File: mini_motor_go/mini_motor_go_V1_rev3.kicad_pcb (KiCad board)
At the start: 4 copper layers, 72 x 47 mm, 83 parts, among them J1 CONN_03POLAR_LOCK, J10 Conn_01x02_Pin, J11 USB4520-03-0-A_REVA, J12 BM05B-SRSS-TB_LF__SN_, J13 BM05B-SRSS-TB_LF__SN_, J2 CONN_03POLAR_LOCK, J3 I2C_STANDARDQWIIC, J5 I2C_STANDARDQWIIC, J9 Conn_01x09_Pin, U1 ESP32-S3-WROOM-1, U2 TMC6300, U3 INA2181, U4 INA2181, U5 TMC6300, U6 AZ1117C, U7 TPS562208

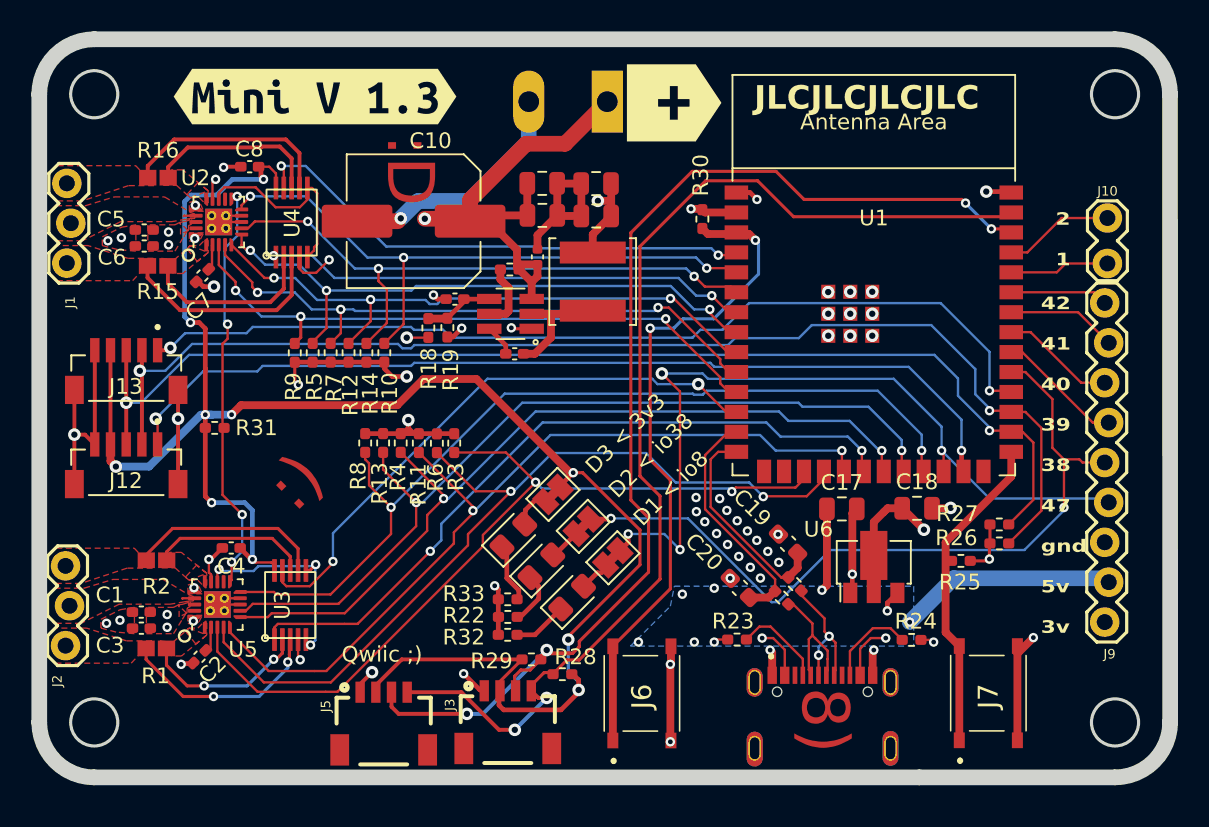
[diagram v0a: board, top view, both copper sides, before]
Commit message: reviewed value table in schematics, updated footprints on board minor improvements
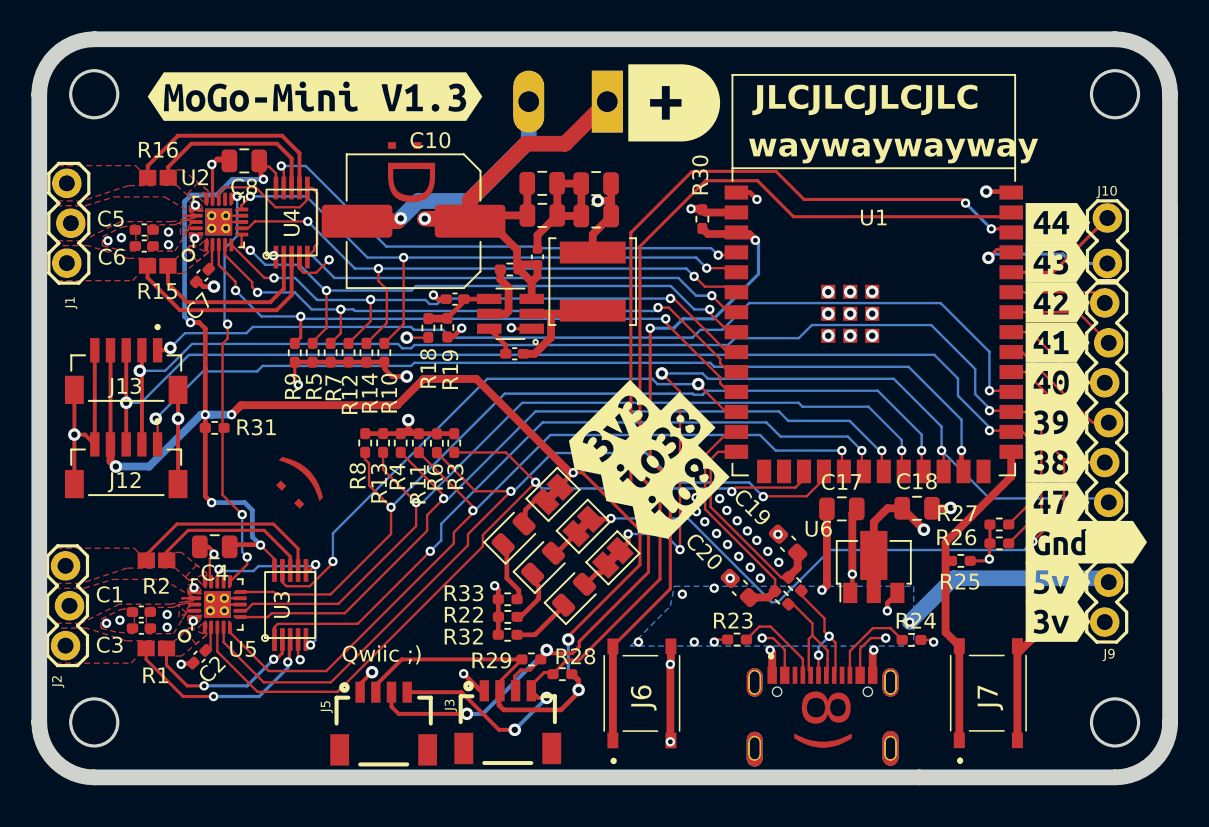
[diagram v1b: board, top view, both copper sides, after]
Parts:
- removed D1 < io8: LED, mg_mini_v1r3:LED_0805_2012Metric_Pad1.15x1.40mm_HandSolder
- removed D2 < io38: LED, mg_mini_v1r3:LED_0805_2012Metric_Pad1.15x1.40mm_HandSolder
- removed D3 < 3v3: LED, mg_mini_v1r3:LED_0805_2012Metric_Pad1.15x1.40mm_HandSolder
- removed kibuzzard-656F4911: G***, mg_mini_v1r3:kibuzzard-656F4911
- removed kibuzzard-656F59A7: G***, mg_mini_v1r3:kibuzzard-656F59A7
- added D1: LED, LED_SMD:LED_0805_2012Metric, F.Cu at (148.6, 84.9)
- added D2: LED, LED_SMD:LED_0805_2012Metric, F.Cu at (146.6, 82.9)
- added D3: LED, LED_SMD:LED_0805_2012Metric, F.Cu at (144.7, 81.0)
- added kibuzzard-6573395A: G***, kibuzzard-6573395A, F.Cu at (150.9, 74.6)
- added kibuzzard-65733965: G***, kibuzzard-65733965, F.Cu at (153.5, 76.0)
- added kibuzzard-65733972: G***, kibuzzard-65733972, F.Cu at (155.0, 78.6)
- added kibuzzard-65733A0D: G***, kibuzzard-65733A0D, F.Cu at (179.3, 63.7)
- added kibuzzard-65733A1B: G***, kibuzzard-65733A1B, F.Cu at (179.4, 61.2)
- added kibuzzard-65733C02: G***, kibuzzard-65733C02, F.Cu at (179.4, 66.3)
- added kibuzzard-65733C12: G***, kibuzzard-65733C12, F.Cu at (179.3, 68.8)
- added kibuzzard-65733C20: G***, kibuzzard-65733C20, F.Cu at (179.4, 71.4)
- added kibuzzard-65733C2B: G***, kibuzzard-65733C2B, F.Cu at (179.3, 73.9)
- added kibuzzard-65733C3A: G***, kibuzzard-65733C3A, F.Cu at (179.3, 76.4)
- added kibuzzard-65733C45: G***, kibuzzard-65733C45, F.Cu at (179.3, 79.0)
- added kibuzzard-65733C60: G***, kibuzzard-65733C60, F.Cu at (179.4, 84.1)
- added kibuzzard-65733C66: G***, kibuzzard-65733C66, F.Cu at (179.4, 86.6)
- added kibuzzard-65733C85: G***, kibuzzard-65733C85, F.Cu at (181.2, 81.5)
- added kibuzzard-65733FCF: G***, kibuzzard-65733FCF, F.Cu at (132.1, 53.1)
- added kibuzzard-65733FF1: G***, kibuzzard-65733FF1, F.Cu at (154.9, 53.5)
- C1, C2, C5, C7: value 10NF-0603-50V-10% -> 10NF
- C4, C8: footprint mg_mini_v1r3:C_0402_1005Metric_Pad0.74x0.62mm_HandSolder -> Capacitor_SMD:C_0805_2012Metric
- moved C4 1.05 mm to (125.7, 81.8)
- moved C8 0.50 mm to (127.6, 57.2)
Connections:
- U1 pad 36: Net-(J10-Pin_1) -> Net-(J10-Pin_2)
- U1 pad 37: Net-(J10-Pin_2) -> Net-(J10-Pin_1)
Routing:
- net Net-(J10-Pin_1): track 6.36 -> 9.67 mm, vias 0 -> 1
- net GND: track 103.9 -> 106.6 mm, vias 61 -> 60
- net +3.3V: track 136.4 -> 137.1 mm
- net Net-(J10-Pin_2): track 7.03 -> 7.56 mm
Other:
- board text added: "waywaywayway"
- board text removed: "2 1"
- board text removed: "42 41 40 39 38 47 gnd 5v 3v"
